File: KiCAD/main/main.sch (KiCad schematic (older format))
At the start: 17 parts, among them IC1 DHT22, J1 Sound Sensor, J2 BuckConverter, J3 Charge Controller, J4 Battery Status, J5 Anemometer, SW1 SW_SPDT, U1 4020, U2 4N25

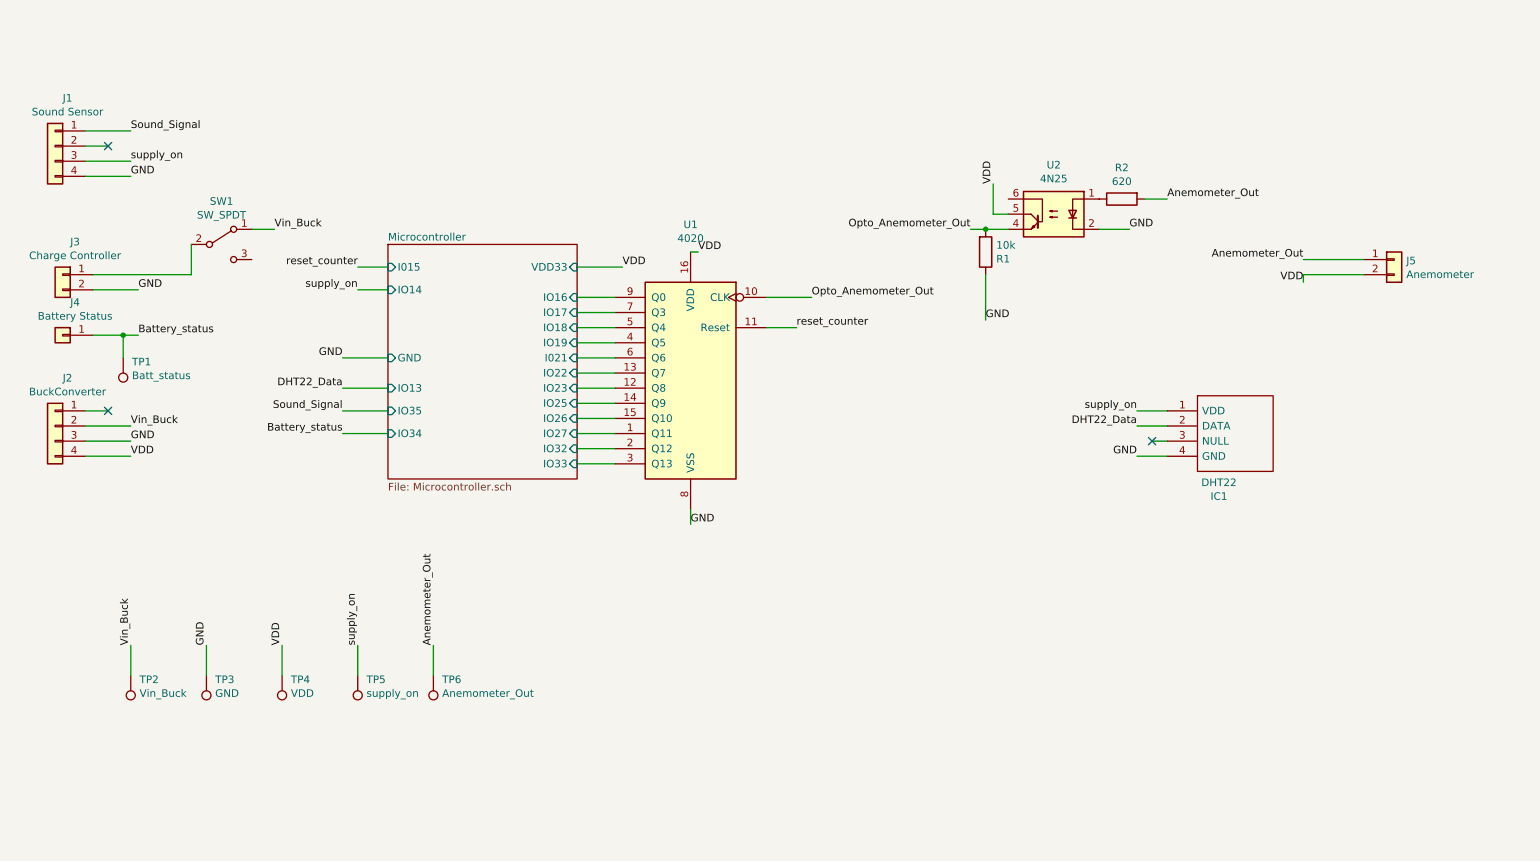
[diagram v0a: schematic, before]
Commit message: Replace DHT22 and cound sensor JST connector with GROVE connectors
Also replace mounting holes and add them to the reference schematic
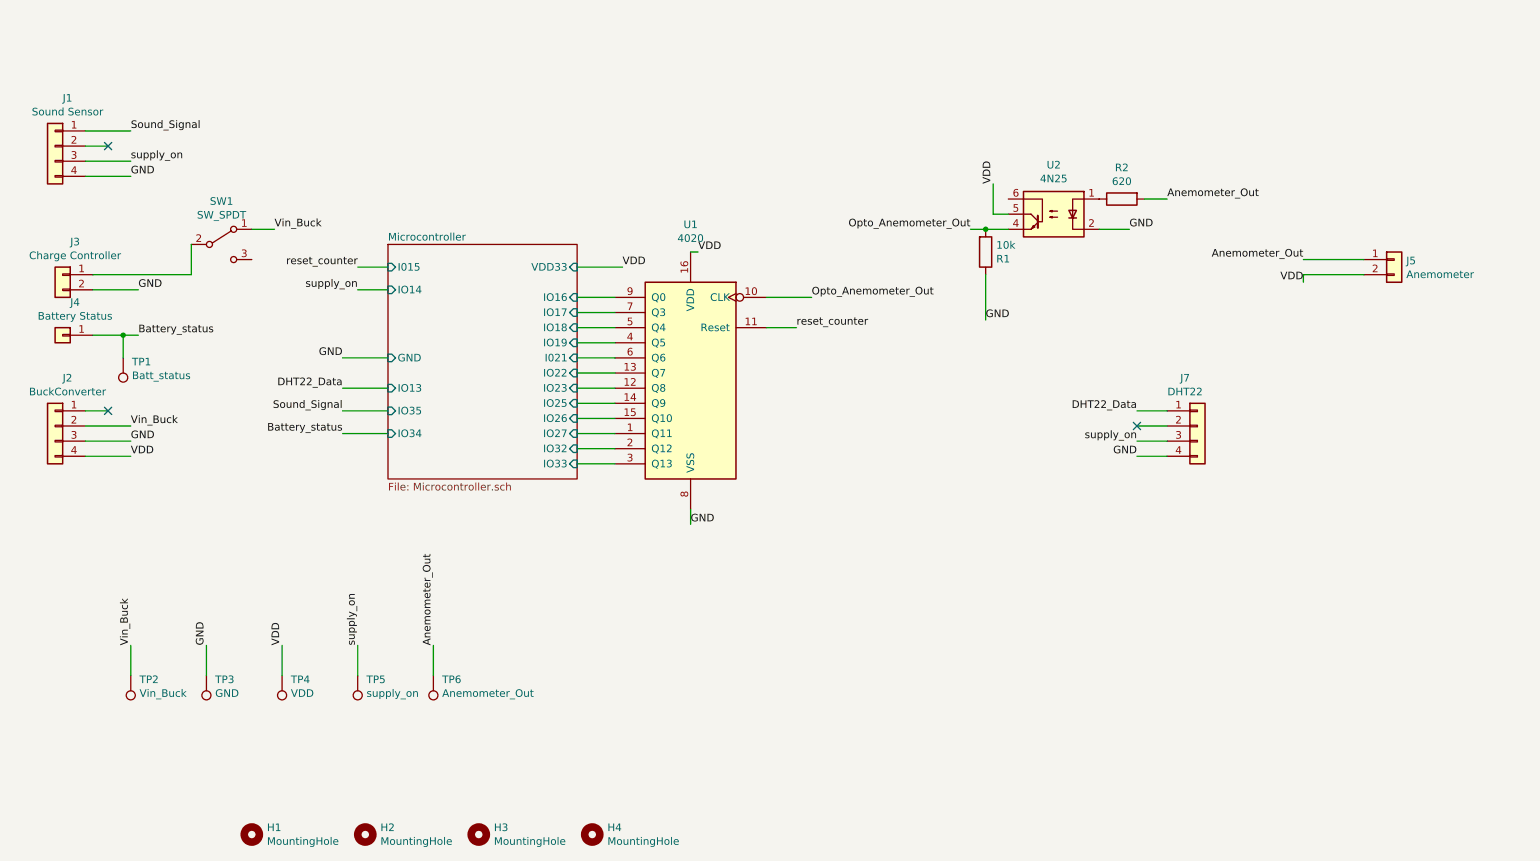
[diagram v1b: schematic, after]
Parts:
- removed IC1: DHT22, Local:DHT22, symbol DHT22:DHT22
- added H1, H2, H3, H4: MountingHole, MountingHole:MountingHole_3.2mm_M3_Pad, symbol Mechanical:MountingHole
- added J7: DHT22, Connector:NS-Tech_Grove_1x04_P2mm_Vertical, symbol Connector_Generic:Conn_01x04
- J1: footprint Connector_JST:JST_PH_B4B-PH-K_1x04_P2.00mm_Vertical -> Connector:NS-Tech_Grove_1x04_P2mm_Vertical
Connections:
- net DHT22_Data: now also J7.1 (Pin_1)
- net GND: now also J7.4 (Pin_4)
- net supply_on: now also J7.3 (Pin_3)
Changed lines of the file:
@@
 F 0 "J1" H 918 2167 50  0000 C CNN
 F 1 "Sound Sensor" H 918 2076 50  0000 C CNN
-F 2 "Connector_JST:JST_PH_B4B-PH-K_1x04_P2.00mm_Vertical" H 1000 1850 50  0001 C CNN
+F 2 "Connector:NS-Tech_Grove_1x04_P2mm_Vertical" H 1000 1850 50  0001 C CNN
 F 3 "~" H 1000 1850 50  0001 C CNN
 	1    1000 1850
@@
 Text Label 8150 3900 2    50   ~ 0
 GND
-Text Label 8150 3700 2    50   ~ 0
+Text Label 8150 3600 2    50   ~ 0
 DHT22_Data
 Wire Wire Line
-	8350 3800 8250 3800
-NoConn ~ 8250 3800
-Wire Wire Line
 	8350 3900 8150 3900
 Wire Wire Line
 	8350 3700 8150 3700
-$Comp
-L DHT22:DHT22 IC1
-U 1 1 5FB3BE3A
-P 8350 3600
-F 0 "IC1" H 8692 3035 50  0000 C CNN
-F 1 "DHT22" H 8692 3126 50  0000 C CNN
-F 2 "Local:DHT22" H 9100 3700 50  0001 L CNN
-F 3 "https://datasheet4u.com/datasheet-parts/DHT22-datasheet.php?id=792211" H 9100 3600 50  0001 L CNN
-F 4 "Digital-output relative humidity & temperature sensor/module DHT22" H 9100 3500 50  0001 L CNN "Description"
-F 5 "25.1" H 9100 3400 50  0001 L CNN "Height"
-F 6 "Aosong Electronics" H 9100 3300 50  0001 L CNN "Manufacturer_Name"
-F 7 "DHT22" H 9100 3200 50  0001 L CNN "Manufacturer_Part_Number"
-F 8 "" H 9100 3100 50  0001 L CNN "Arrow Part Number"
-F 9 "" H 9100 3000 50  0001 L CNN "Arrow Price/Stock"
-F 10 "" H 9100 2900 50  0001 L CNN "Mouser Part Number"
-F 11 "" H 9100 2800 50  0001 L CNN "Mouser Price/Stock"
-	1    8350 3600
-	1    0    0    -1
-$EndComp
 $Sheet
 S 3200 2500 1250 1550
@@
 Wire Wire Line
 	8350 3600 8150 3600
-Text Label 8150 3600 2    50   ~ 0
+Text Label 8150 3800 2    50   ~ 0
 supply_on
 Wire Wire Line
@@
 	0    -1   1    0
 $EndComp
+$Comp
+L Connector_Generic:Conn_01x04 J7
+U 1 1 5FF3154C
+P 8550 3700
+F 0 "J7" H 8468 4017 50  0000 C CNN
+F 1 "DHT22" H 8468 3926 50  0000 C CNN
+F 2 "Connector:NS-Tech_Grove_1x04_P2mm_Vertical" H 8550 3700 50  0001 C CNN
+F 3 "~" H 8550 3700 50  0001 C CNN
+	1    8550 3700
+	1    0    0    -1
+$EndComp
+NoConn ~ 8150 3700
+Wire Wire Line
+	8150 3800 8350 3800
+$Comp
+L Mechanical:MountingHole H1
+U 1 1 5FF3F11A
+P 2300 6400
+F 0 "H1" H 2400 6446 50  0000 L CNN
+F 1 "MountingHole" H 2400 6355 50  0000 L CNN
+F 2 "MountingHole:MountingHole_3.2mm_M3_Pad" H 2300 6400 50  0001 C CNN
+F 3 "~" H 2300 6400 50  0001 C CNN
+	1    2300 6400
+	1    0    0    -1
+$EndComp
+$Comp
+L Mechanical:MountingHole H2
+U 1 1 5FF3F7F3
+P 3050 6400
+F 0 "H2" H 3150 6446 50  0000 L CNN
+F 1 "MountingHole" H 3150 6355 50  0000 L CNN
+F 2 "MountingHole:MountingHole_3.2mm_M3_Pad" H 3050 6400 50  0001 C CNN
+F 3 "~" H 3050 6400 50  0001 C CNN
+	1    3050 6400
+	1    0    0    -1
+$EndComp
+$Comp
+L Mechanical:MountingHole H3
+U 1 1 5FF3FB3A
+P 3800 6400
+F 0 "H3" H 3900 6446 50  0000 L CNN
+F 1 "MountingHole" H 3900 6355 50  0000 L CNN
+F 2 "MountingHole:MountingHole_3.2mm_M3_Pad" H 3800 6400 50  0001 C CNN
+F 3 "~" H 3800 6400 50  0001 C CNN
+	1    3800 6400
+	1    0    0    -1
+$EndComp
+$Comp
+L Mechanical:MountingHole H4
+U 1 1 5FF3FF6B
+P 4550 6400
+F 0 "H4" H 4650 6446 50  0000 L CNN
+F 1 "MountingHole" H 4650 6355 50  0000 L CNN
+F 2 "MountingHole:MountingHole_3.2mm_M3_Pad" H 4550 6400 50  0001 C CNN
+F 3 "~" H 4550 6400 50  0001 C CNN
+	1    4550 6400
+	1    0    0    -1
+$EndComp
 $EndSCHEMATC

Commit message: Increase margins for the fixtures
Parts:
- J5: footprint Connector_JST:JST_PH_B2B-PH-K_1x02_P2.00mm_Vertical -> Connector_RJ:RJ14_Connfly_DS1133-S4_Horizontal; symbol Connector_Generic:Conn_01x02 -> Connector:4P4C
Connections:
- net Anemometer_Out: now also J5.3; no longer J5.1 (Pin_1)
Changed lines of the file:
@@
 Wire Wire Line
 	4750 2650 4450 2650
-Wire Wire Line
-	9250 2700 9650 2700
 $Comp
 L Connector_Generic:Conn_01x04 J2
@@
 	1550 2800 1250 2800
 $Comp
-L Connector_Generic:Conn_01x02 J5
+L Connector:4P4C J5
 U 1 1 5FC61584
-P 9850 2600
-F 0 "J5" H 9930 2592 50  0000 L CNN
-F 1 "Anemometer" H 9930 2501 50  0000 L CNN
-F 2 "Connector_JST:JST_PH_B2B-PH-K_1x02_P2.00mm_Vertical" H 9850 2600 50  0001 C CNN
-F 3 "~" H 9850 2600 50  0001 C CNN
-	1    9850 2600
-	1    0    0    -1
+P 10050 2600
+F 0 "J5" H 10250 2350 50  0000 L CNN
+F 1 "Anemometer" H 9750 2350 50  0000 L CNN
+F 2 "Connector_RJ:RJ14_Connfly_DS1133-S4_Horizontal" H 10050 2600 50  0001 C CNN
+F 3 "~" H 10050 2600 50  0001 C CNN
+	1    10050 2600
+	-1   0    0    1
 $EndComp
 Text Label 8150 3900 2    50   ~ 0
@@
 Text Label 3000 2800 2    50   ~ 0
 supply_on
-Wire Wire Line
-	9250 2750 9250 2700
-Text Label 9250 2750 2    50   ~ 0
+Text Label 9250 2600 2    50   ~ 0
 VDD
 Text Label 7150 3000 0    50   ~ 0
@@
 Text Label 8150 3800 2    50   ~ 0
 supply_on
-Wire Wire Line
-	9250 2600 9650 2600
 Wire Wire Line
 	7200 2100 7200 2300
@@
 	-1   0    0    -1
 $EndComp
-Text Label 9250 2600 2    50   ~ 0
+Text Label 9250 2700 2    50   ~ 0
 Anemometer_Out
 Wire Wire Line
@@
 	1    0    0    -1
 $EndComp
+Wire Wire Line
+	9250 2600 9650 2600
+Wire Wire Line
+	9250 2700 9650 2700
 $EndSCHEMATC

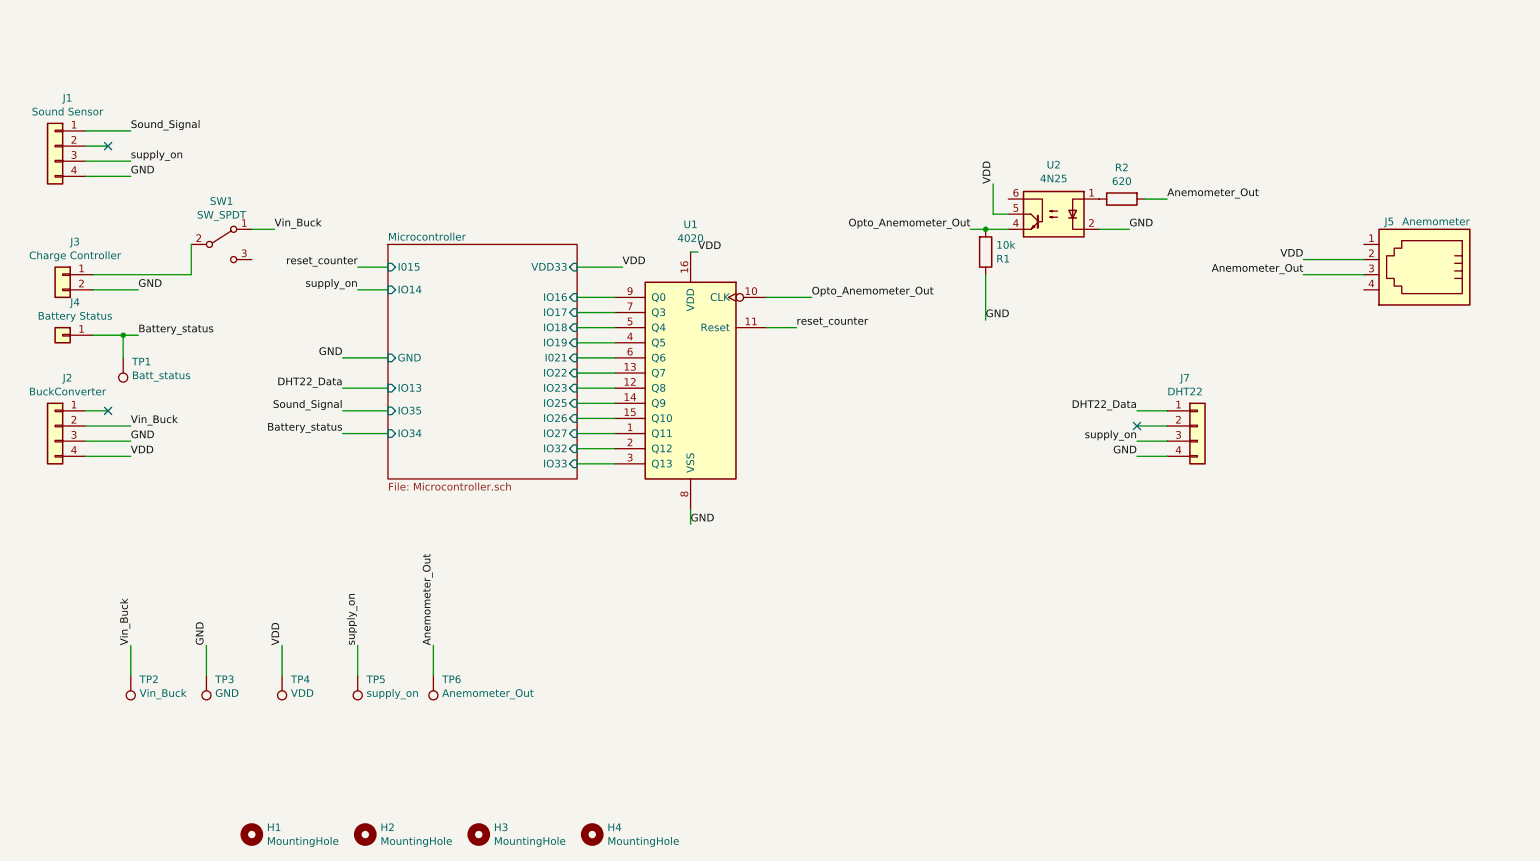
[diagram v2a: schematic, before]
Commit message: Re-annotate connectors
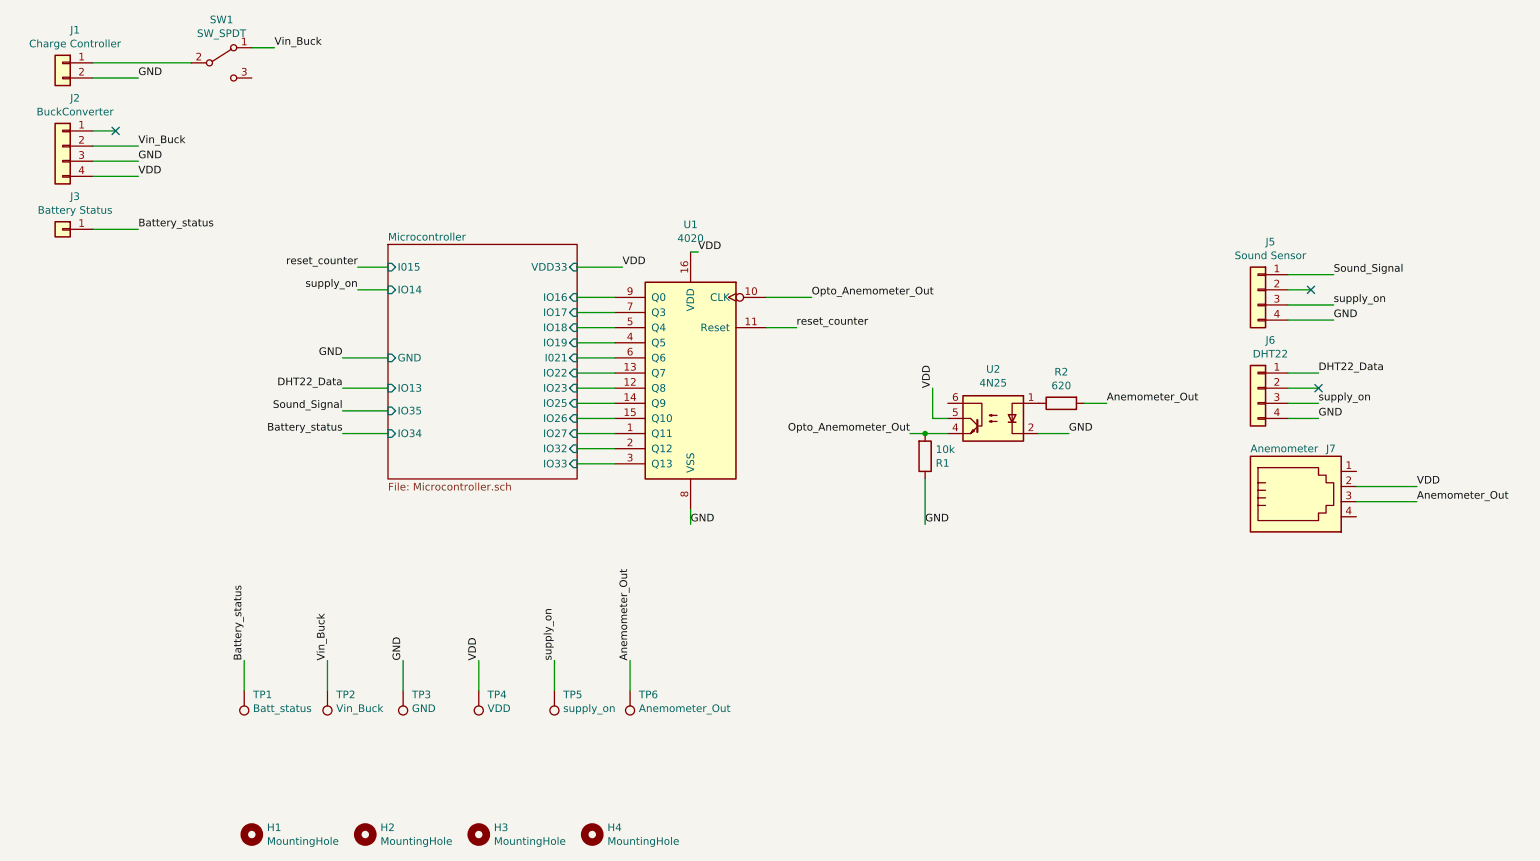
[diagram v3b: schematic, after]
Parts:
- renumbered J3 to J1, J4 to J3, J1 to J5, J7 to J6, J5 to J7
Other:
- moved on the sheet: J1, J2, J3, J5, J6, J7, R1, R2, SW1, TP1, TP2, TP3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
